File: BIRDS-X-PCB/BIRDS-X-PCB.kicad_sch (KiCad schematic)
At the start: 1 part, among them J101 NRPN252PARN-RC or LPC-50M2LG 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

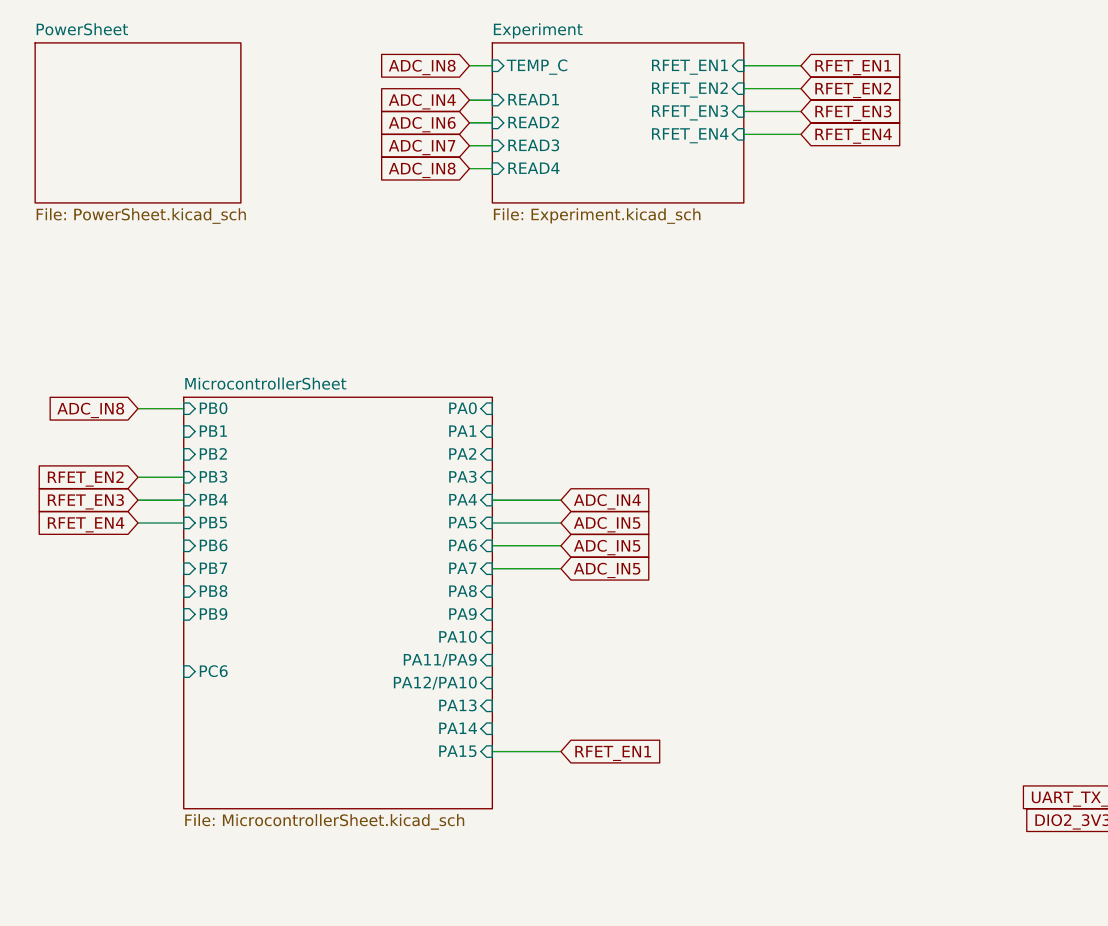
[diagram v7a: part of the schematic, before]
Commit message: Semantic and symbol updates, begin review changes
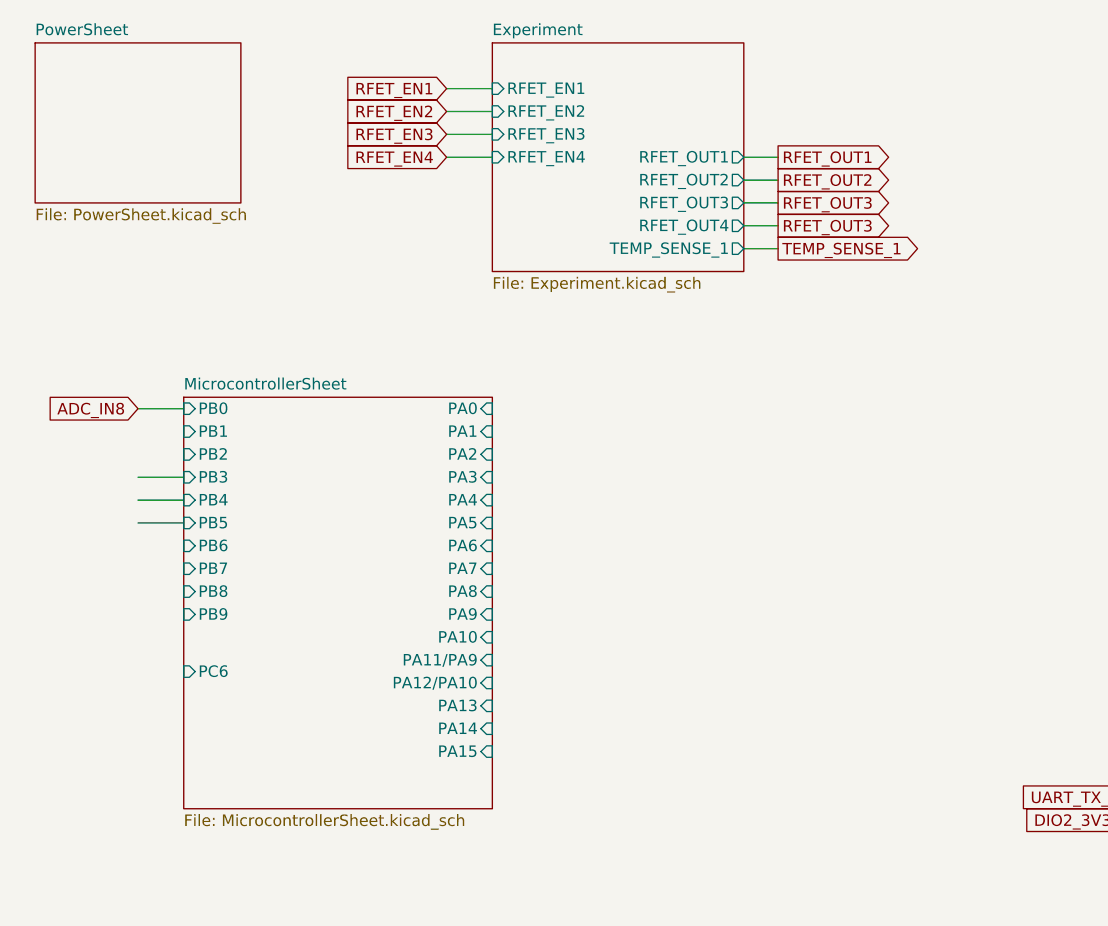
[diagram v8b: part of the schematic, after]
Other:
- sheet Experiment ports: added RFET_OUT1, RFET_OUT2, RFET_OUT3, RFET_OUT4, TEMP_SENSE_1; removed READ1, READ2, READ3, READ4, TEMP_C
